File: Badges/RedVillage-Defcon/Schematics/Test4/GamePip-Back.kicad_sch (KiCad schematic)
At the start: 58 parts, among them J1 2.8" Display, J10 Conn_01x01, J11 Conn_01x01, J12 Conn_01x01, J13 Conn_02x03_Odd_Even, J14 Conn_01x03, J2 USB_C_Plug_USB2.0, J3 Conn_01x03, J4 Cap Sense, J5 Cap Sense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

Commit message: V1 complete
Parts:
- removed C10, C11: 100nF, Capacitor_SMD:C_0805_2012Metric, symbol Device:C_Small
- removed J7: Conn_01x02, Connector_PinSocket_2.54mm:PinSocket_1x02_P2.54mm_Vertical, symbol Connector_Generic:Conn_01x02
- removed U3, U4: SK6812_Side, Bsides22:SK6812_Side, symbol BSides22:SK6812_Side

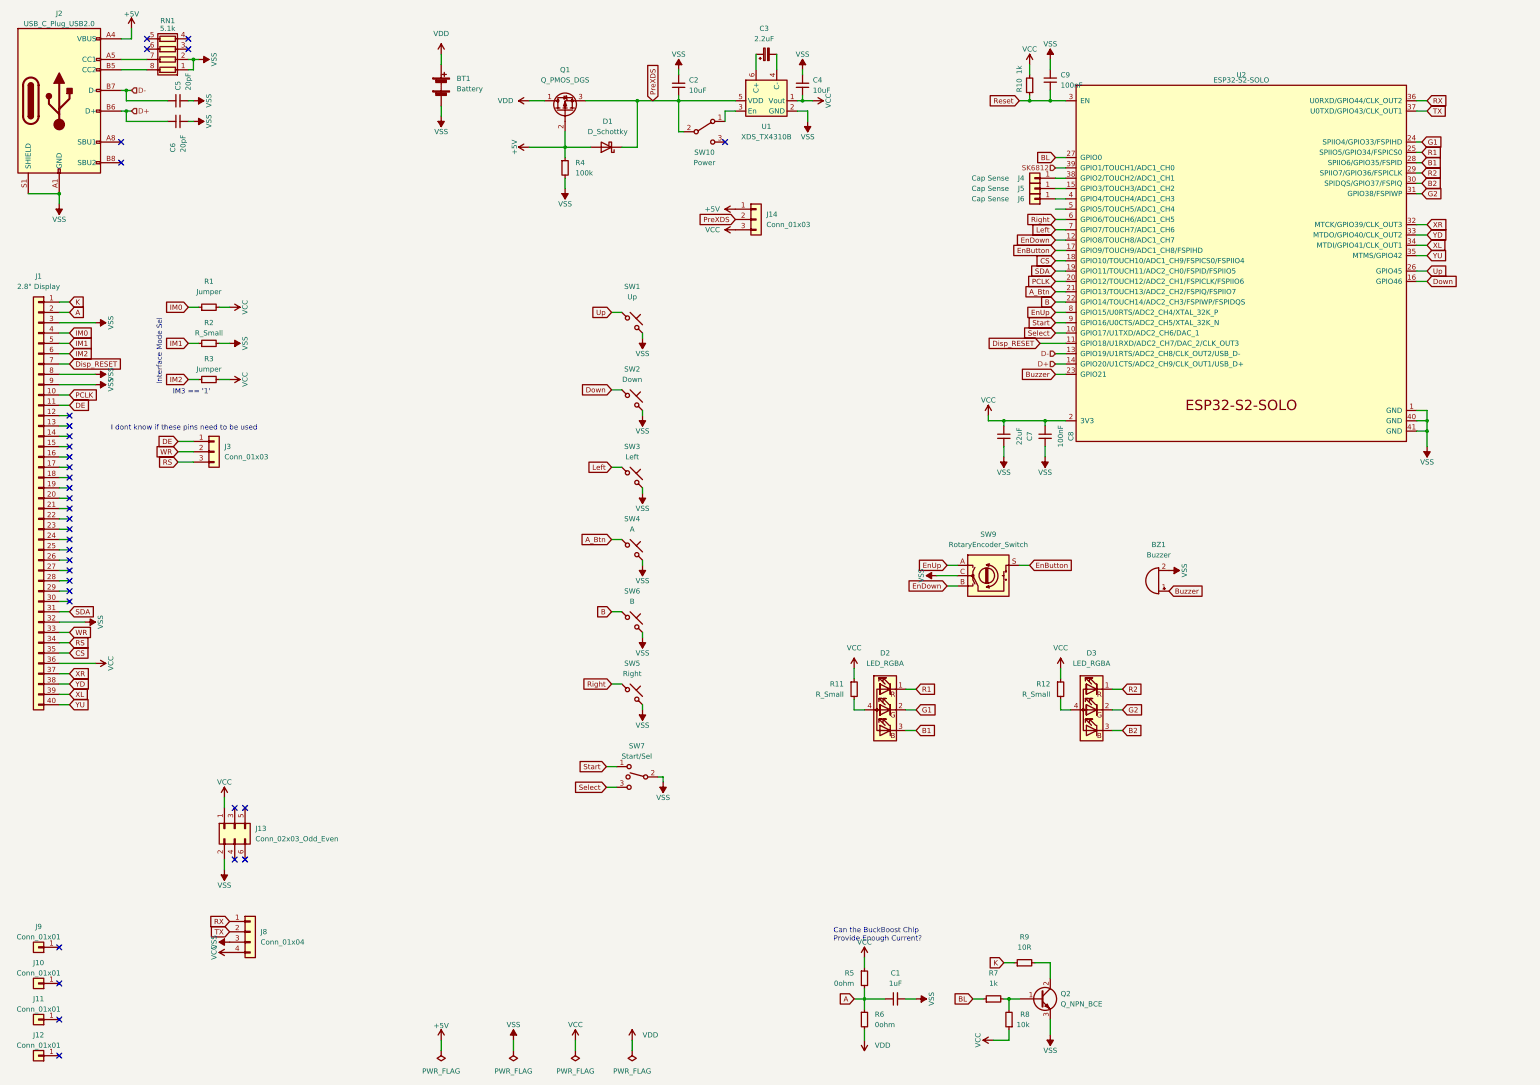
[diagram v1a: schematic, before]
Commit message: Added assembly notes
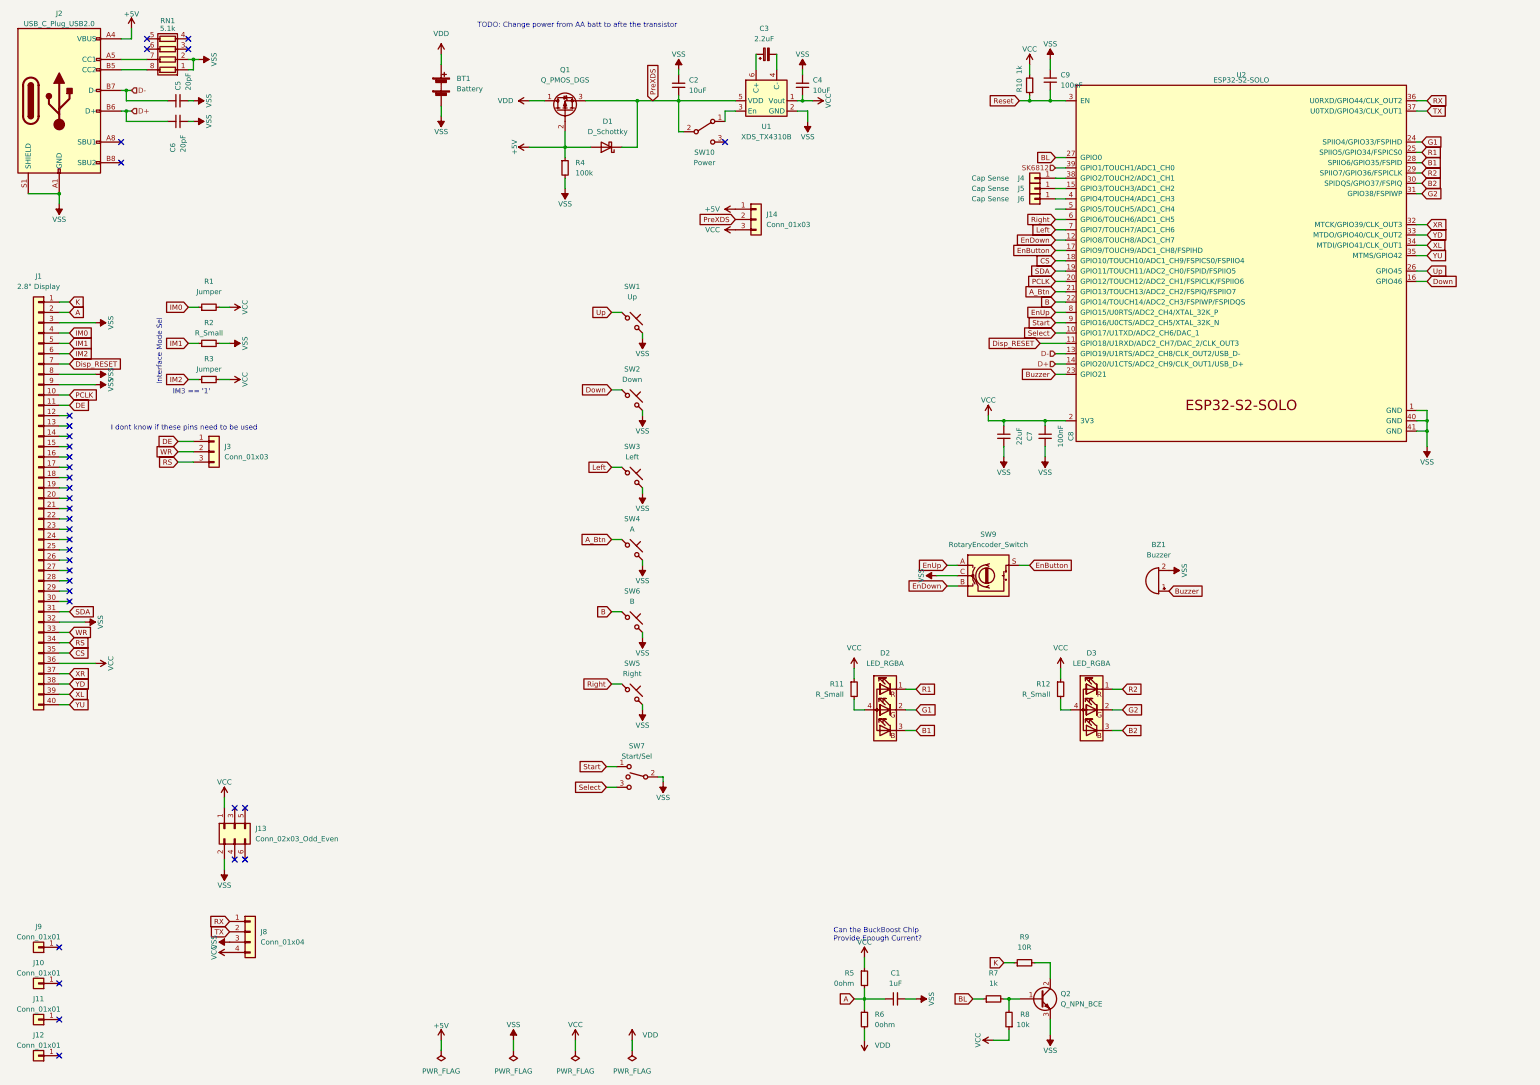
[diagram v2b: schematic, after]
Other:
- note added: "TODO: Change power from AA batt to afte the transistor"
